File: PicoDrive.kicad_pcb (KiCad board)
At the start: 2 copper layers, 72 x 90 mm, 72 parts, among them J1 Conn_01x02, J2 Conn_01x02, J3 Conn_01x02, J4 Conn_01x02, J5 Conn_01x02, J6 Conn_01x02, J7 Conn_01x02, J8 Conn_02x05_Odd_Even, J9 Conn_01x05, Q1 PSMN4R5-30YLC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

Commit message: Add mouser no's, pullup resistor, change project name
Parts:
- added R16: 10k, Resistor_SMD:R_0805_2012Metric_Pad1.20x1.40mm_HandSolder, F.Cu at (167.0, 139.6)
- U2, U3, U4, U5: value DRV8801PWP -> DRV8801PWPR
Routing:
- net /~{EXP1_INT}: track 44.5 -> 66.6 mm, vias 2 -> 4
- net +3V3: track 172.5 -> 174.3 mm
- net /M4_PH: track 94.9 -> 94.0 mm
- net GND1: vias 273 -> 278

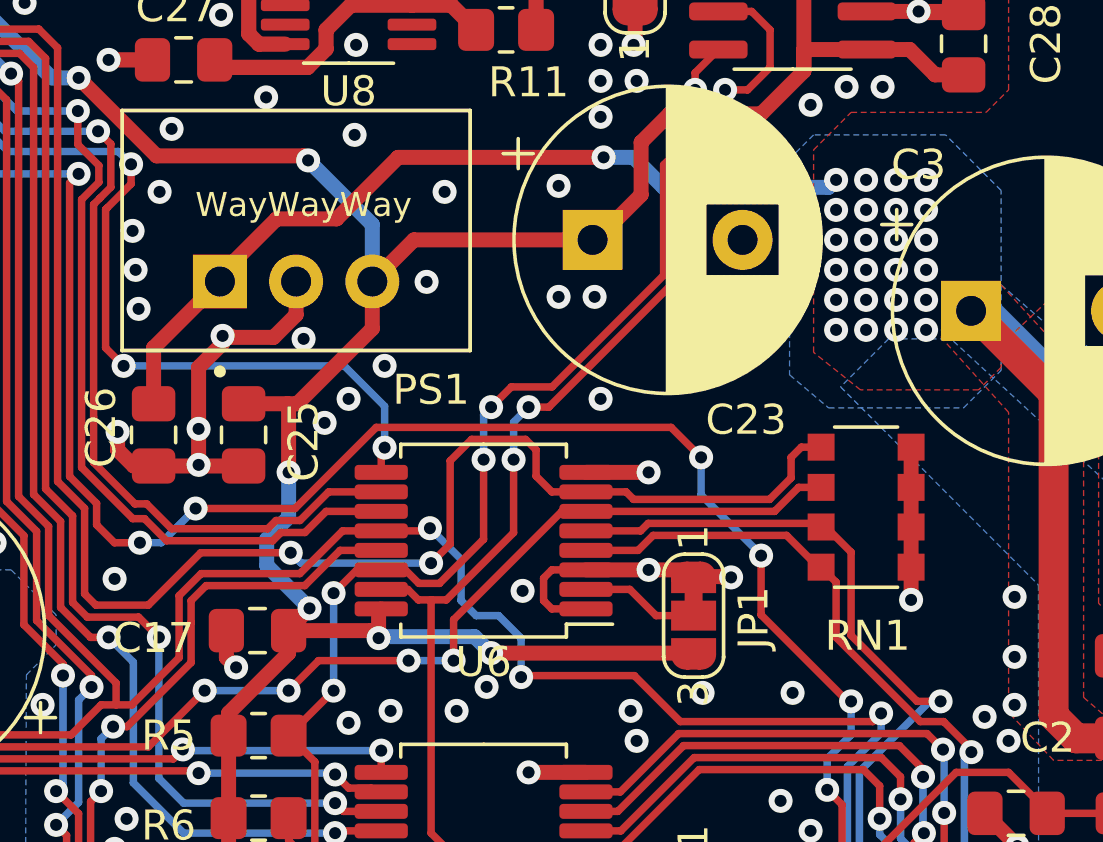
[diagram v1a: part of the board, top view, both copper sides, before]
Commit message: Fix mfault pullup resistor (it was configured as a pulldown)
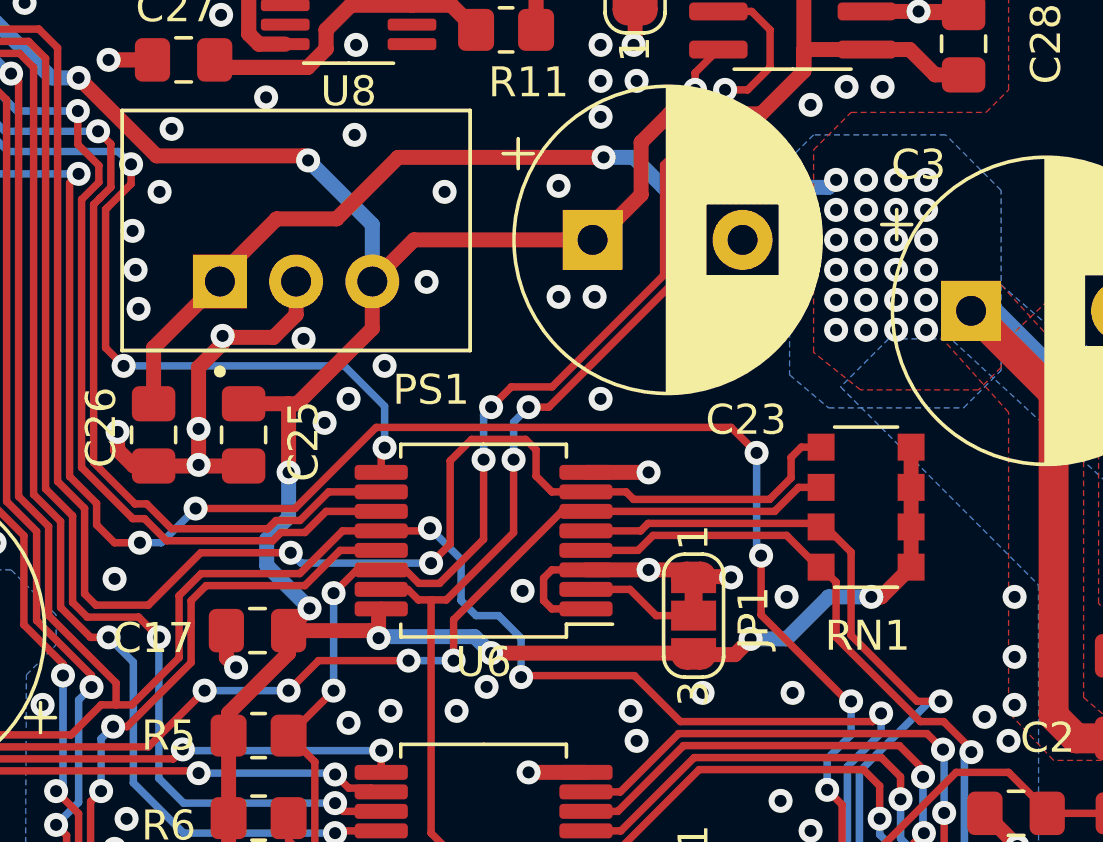
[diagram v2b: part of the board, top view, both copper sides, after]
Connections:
- RN1 pad 1: GND1 -> +3V3
- RN1 pad 2: GND1 -> +3V3
- RN1 pad 3: GND1 -> +3V3
- RN1 pad 4: GND1 -> +3V3
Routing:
- net +3V3: track 174.3 -> 186.8 mm, vias 13 -> 15
- net GND1: track 234.2 -> 229.1 mm
- net /M4_VPROPI: track 97.7 -> 98.9 mm
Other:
- board text removed: "WayWayWay"
